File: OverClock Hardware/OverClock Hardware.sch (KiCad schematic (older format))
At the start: 9 parts, among them J1 USB_C_Plug

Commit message: Chose Buck Converter and added necessary documumentation
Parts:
- added U?: TLV62569, Maxted Libs:SOT23-6, symbol Maxted_Libs:TLV62569
- J1: footprint (none) -> Maxted Libs:Hirose_USB_C_Connector; Vendor (none) -> https://www.digikey.co.nz/product-detail/en/hirose-electric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
- RN1, RN2, RN3, RN4: renamed from RN?; footprint (none) -> Maxted Libs:1506_Array; Vendor (none) -> https://www.digikey.co.nz/product-detail/en/panasonic-elect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
- renumbered D2 to D1, D1 to D2, D4 to D3, D3 to D4
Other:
- moved on the sheet: D2, D3, D4, RN2, RN3, RN4

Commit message: Added in power supply section
Added a Buck converter to drop Vbus (5-20V) down to 4V for LEDs and the the 4V line is dropped further to 3V using a LDO to power the FPGA
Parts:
- added C1, C2: 10uF, Capacitor_SMD:C_0805_2012Metric_Pad1.15x1.40mm_HandSolder, symbol Device:C_Small
- added C3: 1uF, Capacitor_SMD:C_0805_2012Metric_Pad1.15x1.40mm_HandSolder, symbol Device:C_Small
- added C4: 4.7uF, Capacitor_SMD:C_0805_2012Metric_Pad1.15x1.40mm_HandSolder, symbol Device:C_Small
- added L1: 2.2uH, Maxted Libs:IHLP3232, symbol pspice:INDUCTOR
- added R1: 652K, Resistor_SMD:R_0805_2012Metric_Pad1.15x1.40mm_HandSolder, symbol Device:R_Small
- added R2: 100K, Resistor_SMD:R_0805_2012Metric_Pad1.15x1.40mm_HandSolder, symbol Device:R_Small
- added U2: AP7365, Maxted Libs:SOT-23-5, symbol Maxted_Libs:AP7365
- gave numbers to parts that had none: 1
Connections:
- net labels added: +3V, +4V
- net labels removed: +3V3
- wire segments 104 -> 133
- no-connect marks 16 -> 17
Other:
- note added: "Using a fixed 3V LDO"
- moved on the sheet: U1
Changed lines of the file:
@@
-	1    0    0    -1
-$EndComp
-$Comp
-L power:+3V3 #PWR03
-U 1 1 5C5A2CD8
-P 6150 2550
-F 0 "#PWR03" H 6150 2400 50  0001 C CNN
-F 1 "+3V3" H 6165 2723 50  0000 C CNN
-F 2 "" H 6150 2550 50  0001 C CNN
-F 3 "" H 6150 2550 50  0001 C CNN
-	1    6150 2550
-	1    0    0    -1
-$EndComp
-$Comp
-L power:+3V3 #PWR02
-U 1 1 5C5A2D18
-P 9800 2500
-F 0 "#PWR02" H 9800 2350 50  0001 C CNN
-F 1 "+3V3" H 9815 2673 50  0000 C CNN
-F 2 "" H 9800 2500 50  0001 C CNN
-F 3 "" H 9800 2500 50  0001 C CNN
-	1    9800 2500
-	1    0    0    -1
-$EndComp
-$Comp
-L power:+3V3 #PWR06
-U 1 1 5C5A2D49
-P 9900 4600
-F 0 "#PWR06" H 9900 4450 50  0001 C CNN
-F 1 "+3V3" H 9915 4773 50  0000 C CNN
-F 2 "" H 9900 4600 50  0001 C CNN
-F 3 "" H 9900 4600 50  0001 C CNN
-	1    9900 4600
-	1    0    0    -1
-$EndComp
-$Comp
-L power:+3V3 #PWR05
-U 1 1 5C5A2D7A
-P 6150 4600
-F 0 "#PWR05" H 6150 4450 50  0001 C CNN
-F 1 "+3V3" H 6165 4773 50  0000 C CNN
-F 2 "" H 6150 4600 50  0001 C CNN
-F 3 "" H 6150 4600 50  0001 C CNN
-	1    6150 4600
 	1    0    0    -1
 $EndComp
 Wire Wire Line
 	6050 4600 6150 4600
-Connection ~ 6150 4600
 Wire Wire Line
 	6050 2550 6150 2550
-Connection ~ 6150 2550
 Wire Wire Line
 	9700 2500 9800 2500
-Connection ~ 9800 2500
 Wire Wire Line
 	9800 4600 9900 4600
-Connection ~ 9900 4600
 $Comp
 L Device:R_Pack08 RN2
@@
 	8900 6150 9150 6150
 $Comp
-L Maxted_Libs:TLV62569 U?
+L Maxted_Libs:TLV62569 U1
 U 1 1 5C5DF1C9
-P 3200 1650
-F 0 "U?" H 3250 2125 50  0000 C CNN
-F 1 "TLV62569" H 3250 2034 50  0000 C CNN
-F 2 "Maxted Libs:SOT23-6" H 2850 1350 50  0001 C CNN
-F 3 "http://www.ti.com/lit/ds/symlink/tlv62569.pdf" H 2850 1200 50  0001 C CNN
-	1    3200 1650
-	1    0    0    -1
-$EndComp
+P 3050 1000
+F 0 "U1" H 3100 1475 50  0000 C CNN
+F 1 "TLV62569" H 3100 1384 50  0000 C CNN
+F 2 "Maxted Libs:SOT23-6" H 2700 700 50  0001 C CNN
+F 3 "http://www.ti.com/lit/ds/symlink/tlv62569.pdf" H 2700 550 50  0001 C CNN
+	1    3050 1000
+	1    0    0    -1
+$EndComp
+Connection ~ 1200 750
+NoConn ~ 2800 1200
+$Comp
+L power:GND #PWR03
+U 1 1 5C5DC52A
+P 3200 1350
+F 0 "#PWR03" H 3200 1100 50  0001 C CNN
+F 1 "GND" H 3205 1177 50  0000 C CNN
+F 2 "" H 3200 1350 50  0001 C CNN
+F 3 "" H 3200 1350 50  0001 C CNN
+	1    3200 1350
+	1    0    0    -1
+$EndComp
+$Comp
+L pspice:INDUCTOR L1
+U 1 1 5C5DC5D8
+P 3650 750
+F 0 "L1" H 3650 965 50  0000 C CNN
+F 1 "2.2uH" H 3650 874 50  0000 C CNN
+F 2 "Maxted Libs:IHLP3232" H 3650 750 50  0001 C CNN
+F 3 "http://www.vishay.com/docs/34316/ihlp-3232dz-01.pdf" H 3650 750 50  0001 C CNN
+	1    3650 750
+	1    0    0    -1
+$EndComp
+$Comp
+L Device:R_Small R1
+U 1 1 5C5DC82F
+P 4000 850
+F 0 "R1" H 4059 896 50  0000 L CNN
+F 1 "652K" H 4059 805 50  0000 L CNN
+F 2 "Resistor_SMD:R_0805_2012Metric_Pad1.15x1.40mm_HandSolder" H 4000 850 50  0001 C CNN
+F 3 "~" H 4000 850 50  0001 C CNN
+	1    4000 850
+	1    0    0    -1
+$EndComp
+$Comp
+L Device:R_Small R2
+U 1 1 5C5DC89B
+P 4000 1050
+F 0 "R2" H 4059 1096 50  0000 L CNN
+F 1 "100K" H 4059 1005 50  0000 L CNN
+F 2 "Resistor_SMD:R_0805_2012Metric_Pad1.15x1.40mm_HandSolder" H 4000 1050 50  0001 C CNN
+F 3 "~" H 4000 1050 50  0001 C CNN
+	1    4000 1050
+	1    0    0    -1
+$EndComp
+Connection ~ 4000 950
+Wire Wire Line
+	4000 1350 4000 1150
+Wire Wire Line
+	4000 750  4550 750
+$Comp
+L Device:C_Small C1
+U 1 1 5C5E7528
+P 4550 1000
+F 0 "C1" H 4642 1046 50  0000 L CNN
+F 1 "10uF" H 4642 955 50  0000 L CNN
+F 2 "Capacitor_SMD:C_0805_2012Metric_Pad1.15x1.40mm_HandSolder" H 4550 1000 50  0001 C CNN
+F 3 "~" H 4550 1000 50  0001 C CNN
+	1    4550 1000
+	1    0    0    -1
+$EndComp
+$Comp
+L Device:C_Small C2
+U 1 1 5C5E75D6
+P 4950 1000
+F 0 "C2" H 5042 1046 50  0000 L CNN
+F 1 "10uF" H 5042 955 50  0000 L CNN
+F 2 "Capacitor_SMD:C_0805_2012Metric_Pad1.15x1.40mm_HandSolder" H 4950 1000 50  0001 C CNN
+F 3 "~" H 4950 1000 50  0001 C CNN
+	1    4950 1000
+	1    0    0    -1
+$EndComp
+Wire Wire Line
+	4550 900  4550 750
+Connection ~ 4550 750
+Wire Wire Line
+	4550 750  4950 750
+Wire Wire Line
+	4950 900  4950 750
+Wire Wire Line
+	4950 1100 4950 1350
+Wire Wire Line
+	4950 1350 4550 1350
+Connection ~ 4000 1350
+Wire Wire Line
+	4550 1100 4550 1350
+Connection ~ 4550 1350
+Wire Wire Line
+	4550 1350 4000 1350
+Wire Wire Line
+	3400 950  4000 950
+Wire Wire Line
+	3200 1350 4000 1350
+Connection ~ 3200 1350
+Wire Wire Line
+	3900 750  4000 750
+Connection ~ 4000 750
+$Comp
+L Device:C_Small C4
+U 1 1 5C6080A5
+P 2450 1100
+F 0 "C4" H 2542 1146 50  0000 L CNN
+F 1 "4.7uF" H 2542 1055 50  0000 L CNN
+F 2 "Capacitor_SMD:C_0805_2012Metric_Pad1.15x1.40mm_HandSolder" H 2450 1100 50  0001 C CNN
+F 3 "~" H 2450 1100 50  0001 C CNN
+	1    2450 1100
+	1    0    0    -1
+$EndComp
+Wire Wire Line
+	1200 750  2450 750
+Wire Wire Line
+	2450 1000 2450 950
+Connection ~ 2450 750
+Wire Wire Line
+	2450 750  2800 750
+Wire Wire Line
+	2450 950  2800 950
+Connection ~ 2450 950
+Wire Wire Line
+	2450 950  2450 750
+Wire Wire Line
+	2450 1200 2450 1350
+Wire Wire Line
+	2450 1350 3200 1350
+$Comp
+L power:+4V #PWR02
+U 1 1 5C6155AB
+P 4950 750
+F 0 "#PWR02" H 4950 600 50  0001 C CNN
+F 1 "+4V" H 4965 923 50  0000 C CNN
+F 2 "" H 4950 750 50  0001 C CNN
+F 3 "" H 4950 750 50  0001 C CNN
+	1    4950 750
+	1    0    0    -1
+$EndComp
+Connection ~ 4950 750
+$Comp
+L power:+4V #PWR06
+U 1 1 5C61562E
+P 6150 2550
+F 0 "#PWR06" H 6150 2400 50  0001 C CNN
+F 1 "+4V" H 6165 2723 50  0000 C CNN
+F 2 "" H 6150 2550 50  0001 C CNN
+F 3 "" H 6150 2550 50  0001 C CNN
+	1    6150 2550
+	1    0    0    -1
+$EndComp
+Connection ~ 6150 2550
+$Comp
+L power:+4V #PWR05
+U 1 1 5C615680
+P 9800 2500
+F 0 "#PWR05" H 9800 2350 50  0001 C CNN
+F 1 "+4V" H 9815 2673 50  0000 C CNN
+F 2 "" H 9800 2500 50  0001 C CNN
+F 3 "" H 9800 2500 50  0001 C CNN
+	1    9800 2500
+	1    0    0    -1
+$EndComp
+$Comp
+L power:+4V #PWR08
+U 1 1 5C6156D2
+P 9900 4600
+F 0 "#PWR08" H 9900 4450 50  0001 C CNN
+F 1 "+4V" H 9915 4773 50  0000 C CNN
+F 2 "" H 9900 4600 50  0001 C CNN
+F 3 "" H 9900 4600 50  0001 C CNN
+	1    9900 4600
+	1    0    0    -1
+$EndComp
+$Comp
+L power:+4V #PWR07
+U 1 1 5C615724
+P 6150 4600
+F 0 "#PWR07" H 6150 4450 50  0001 C CNN
+F 1 "+4V" H 6165 4773 50  0000 C CNN
+F 2 "" H 6150 4600 50  0001 C CNN
+F 3 "" H 6150 4600 50  0001 C CNN
+	1    6150 4600
+	1    0    0    -1
+$EndComp
+Connection ~ 6150 4600
+Connection ~ 9900 4600
+Connection ~ 9800 2500
+$Comp
+L Maxted_Libs:AP7365 U2
+U 1 1 5C616624
+P 6500 850
+F 0 "U2" H 6500 1150 50  0000 C CNN
+F 1 "AP7365" H 6500 1050 50  0000 C CNB
+F 2 "Maxted Libs:SOT-23-5" H 6500 300 50  0001 C CNN
+F 3 "https://www.diodes.com/assets/Datasheets/AP7365.pdf" H 6550 200 50  0001 C CNN
+	1    6500 850
+	1    0    0    -1
+$EndComp
+Wire Wire Line
+	4950 750  6050 750
+Wire Wire Line
+	6200 1000 6050 1000
+Wire Wire Line
+	6050 1000 6050 750
+Connection ~ 6050 750
+Wire Wire Line
+	6050 750  6200 750
+Wire Wire Line
+	4950 1350 6500 1350
+Connection ~ 4950 1350
+Text GLabel 7000 750  2    50   Input ~ 0
++3V
+Wire Wire Line
+	7000 750  6900 750
+$Comp
+L Device:C_Small C3
+U 1 1 5C62A7AF
+P 6900 1000
+F 0 "C3" H 6992 1046 50  0000 L CNN
+F 1 "1uF" H 6992 955 50  0000 L CNN
+F 2 "Capacitor_SMD:C_0805_2012Metric_Pad1.15x1.40mm_HandSolder" H 6900 1000 50  0001 C CNN
+F 3 "~" H 6900 1000 50  0001 C CNN
+	1    6900 1000
+	1    0    0    -1
+$EndComp
+Wire Wire Line
+	6900 750  6900 900
+Connection ~ 6900 750
+Wire Wire Line
+	6900 750  6800 750
+Wire Wire Line
+	6900 1100 6900 1350
+Wire Wire Line
+	6900 1350 6500 1350
+Connection ~ 6500 1350
+Text Notes 6900 650  0    50   ~ 0
+Using a fixed 3V LDO
 $EndSCHEMATC

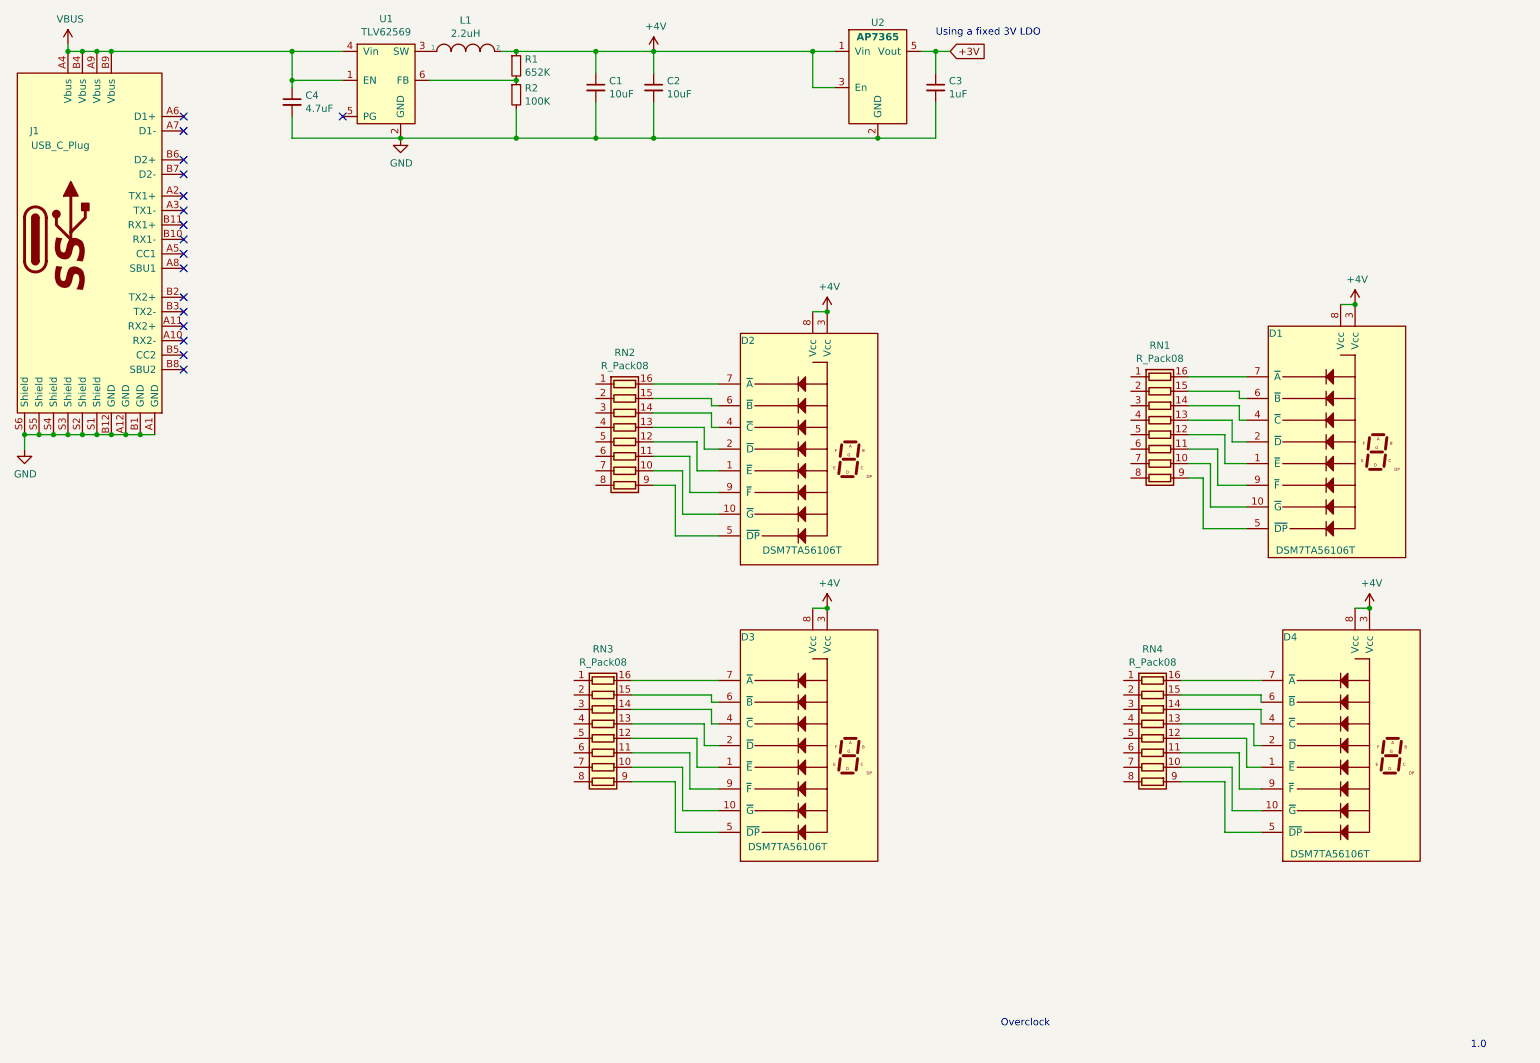
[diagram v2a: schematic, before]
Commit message: Moved Project to Multi-Sheet Design
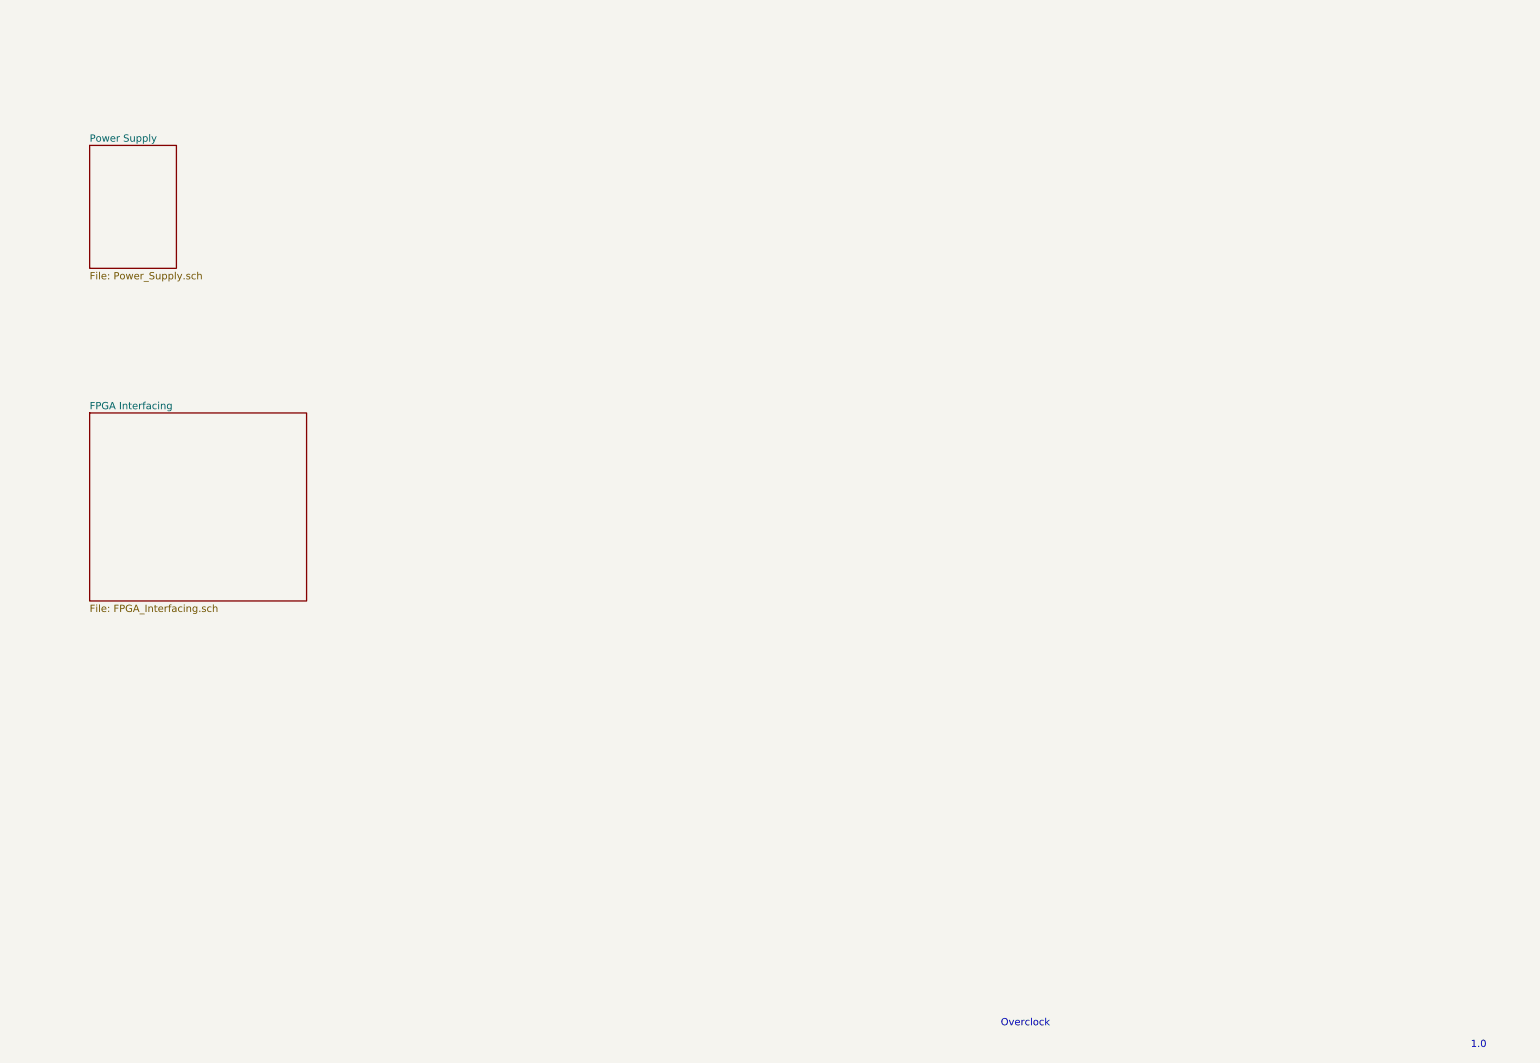
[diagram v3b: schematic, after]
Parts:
- removed C1, C2: 10uF, Capacitor_SMD:C_0805_2012Metric_Pad1.15x1.40mm_HandSolder, symbol Device:C_Small
- removed C3: 1uF, Capacitor_SMD:C_0805_2012Metric_Pad1.15x1.40mm_HandSolder, symbol Device:C_Small
- removed C4: 4.7uF, Capacitor_SMD:C_0805_2012Metric_Pad1.15x1.40mm_HandSolder, symbol Device:C_Small
- removed D1, D2, D3, D4: DSM7TA56106T, symbol Maxted_Libs:DSM7TA56106T
- removed J1: USB_C_Plug, Maxted Libs:Hirose_USB_C_Connector, symbol Maxted_Libs:USB_C_Plug
- removed L1: 2.2uH, Maxted Libs:IHLP3232, symbol pspice:INDUCTOR
- removed R1: 652K, Resistor_SMD:R_0805_2012Metric_Pad1.15x1.40mm_HandSolder, symbol Device:R_Small
- removed R2: 100K, Resistor_SMD:R_0805_2012Metric_Pad1.15x1.40mm_HandSolder, symbol Device:R_Small
- removed RN1, RN2, RN3, RN4: R_Pack08, Maxted Libs:1506_Array, symbol Device:R_Pack08
- removed U1: TLV62569, Maxted Libs:SOT23-6, symbol Maxted_Libs:TLV62569
- removed U2: AP7365, Maxted Libs:SOT-23-5, symbol Maxted_Libs:AP7365
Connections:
- no-connect marks 17 -> 0
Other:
- note removed: "Using a fixed 3V LDO"

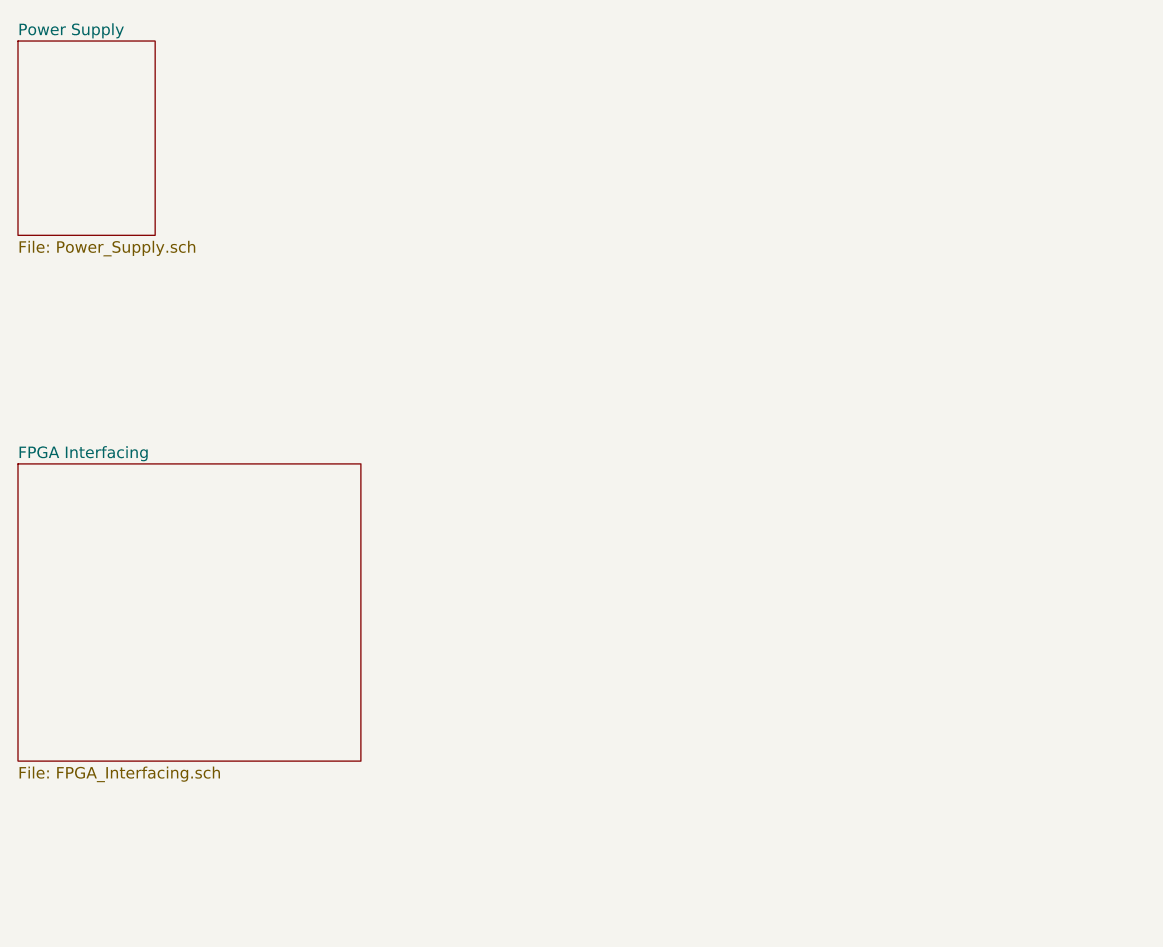
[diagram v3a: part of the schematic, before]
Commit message: Added JTAG Header
Added a JTAG header and interfaced it to the FPGA as per: page 16 https://www.intel.com/content/dam/www/programmable/us/en/pdfs/literature/hb/max-10/m10_guidelines.pdf
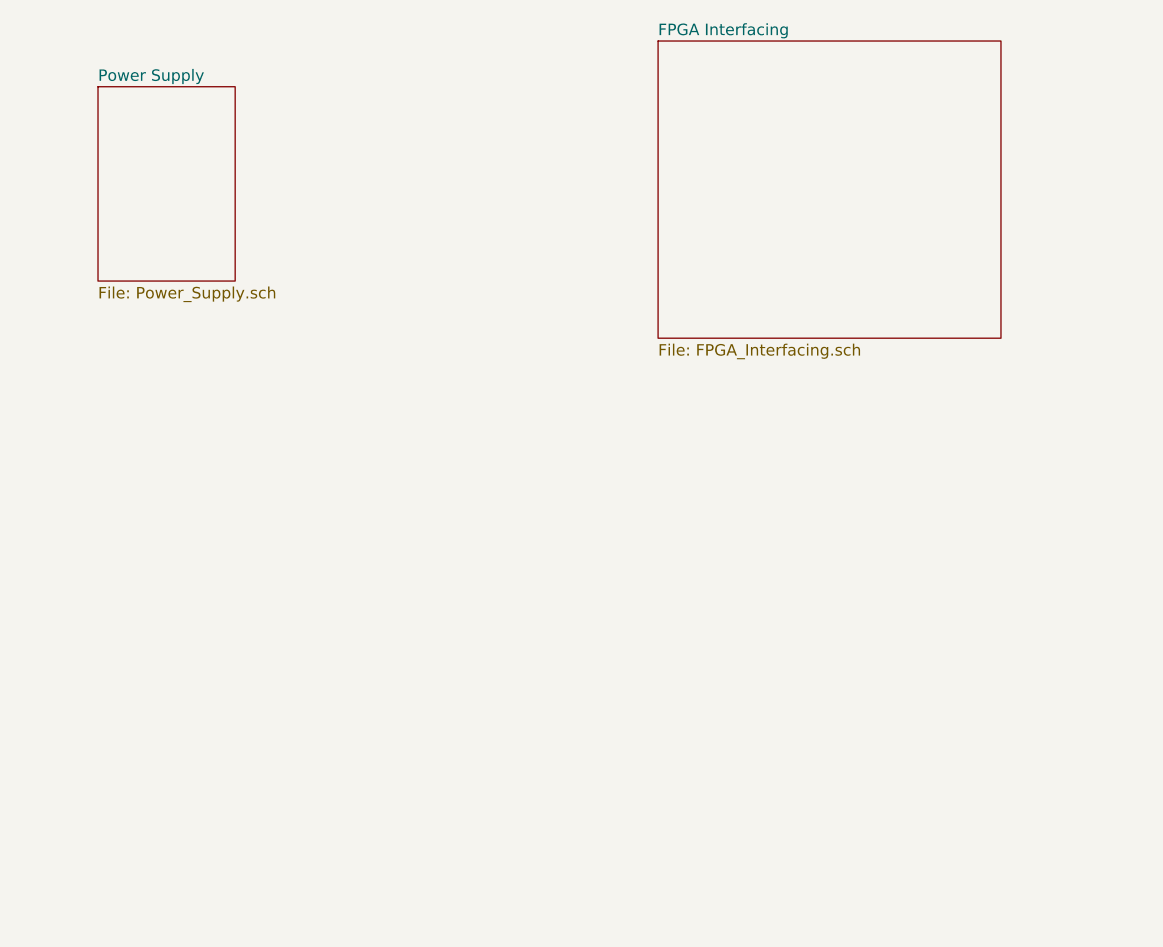
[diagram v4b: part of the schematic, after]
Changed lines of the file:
@@
 1.0
 $Sheet
-S 1050 1400 600  850
+S 1400 1600 600  850
 U 5C656C49
 F0 "Power Supply" 50
@@
 $EndSheet
 $Sheet
-S 1050 3250 1500 1300
+S 3850 1400 1500 1300
 U 5C66B7E8
 F0 "FPGA Interfacing" 50
